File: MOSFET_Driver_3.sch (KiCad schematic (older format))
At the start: 20 parts, among them Q10 TPHR8504PL, Q11 TPHR8504PL, Q12 TPHR8504PL, Q7 TPHR8504PL, Q8 TPHR8504PL, Q9 TPHR8504PL, U1 FD6288Q

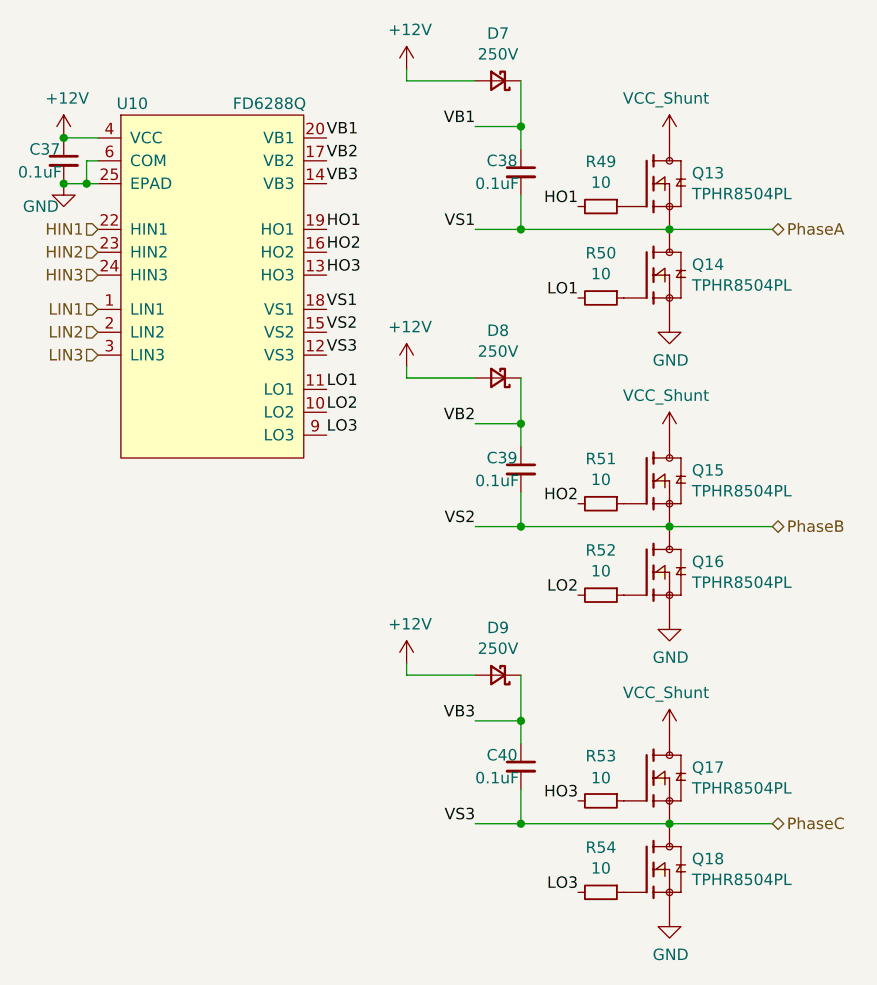
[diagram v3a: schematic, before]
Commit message: Finished all traces and vias
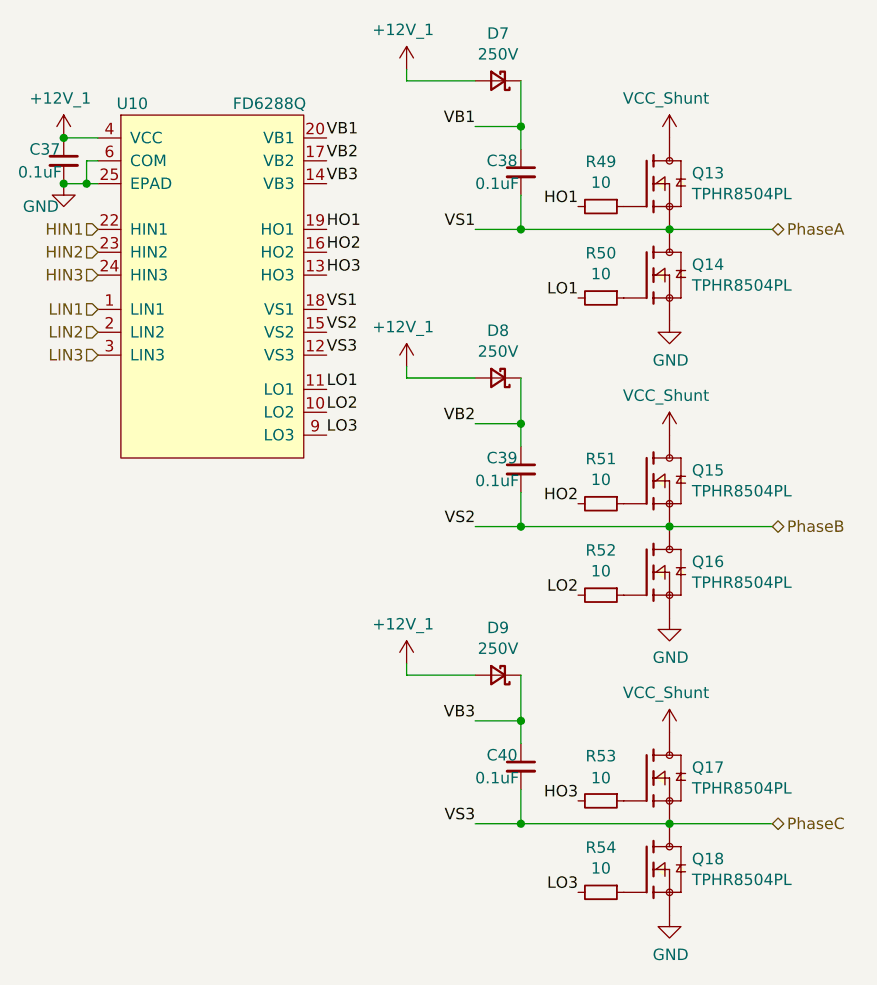
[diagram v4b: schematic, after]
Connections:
- net +12V renamed +12V_1
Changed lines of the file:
@@
 	7500 4850 7500 5000
 Connection ~ 7500 5000
-$Comp
-L power:+12V #PWR02
-U 1 1 6059DFDF
-P 5500 2000
-AR Path="/6035042B/6059DFDF" Ref="#PWR02"  Part="1"
-AR Path="/605793F0/6059DFDF" Ref="#PWR0140"  Part="1"
-AR Path="/6057AB51/6059DFDF" Ref="#PWR0169"  Part="1"
-AR Path="/60597CFF/6059DFDF" Ref="#PWR?"  Part="1"
-AR Path="/60568CDE/6059DFDF" Ref="#PWR0184"  Part="1"
-AR Path="/60595220/6059DFDF" Ref="#PWR0184"  Part="1"
-AR Path="/605CA83C/6059DFDF" Ref="#PWR0184"  Part="1"
-AR Path="/605DC768/6059DFDF" Ref="#PWR0209"  Part="1"
-AR Path="/60536007/6059DFDF" Ref="#PWR0196"  Part="1"
-AR Path="/60551876/6059DFDF" Ref="#PWR0227"  Part="1"
-F 0 "#PWR0196" H 5500 1850 50  0001 C CNN
-F 1 "+12V" H 5515 2173 50  0000 C CNN
-F 2 "" H 5500 2000 50  0001 C CNN
-F 3 "" H 5500 2000 50  0001 C CNN
-	1    5500 2000
-	1    0    0    -1
-$EndComp
-$Comp
-L power:+12V #PWR03
-U 1 1 6059DFE7
-P 7000 3000
-AR Path="/6035042B/6059DFE7" Ref="#PWR03"  Part="1"
-AR Path="/605793F0/6059DFE7" Ref="#PWR0141"  Part="1"
-AR Path="/6057AB51/6059DFE7" Ref="#PWR0170"  Part="1"
-AR Path="/60597CFF/6059DFE7" Ref="#PWR?"  Part="1"
-AR Path="/60568CDE/6059DFE7" Ref="#PWR0185"  Part="1"
-AR Path="/60595220/6059DFE7" Ref="#PWR0185"  Part="1"
-AR Path="/605CA83C/6059DFE7" Ref="#PWR0185"  Part="1"
-AR Path="/605DC768/6059DFE7" Ref="#PWR0210"  Part="1"
-AR Path="/60536007/6059DFE7" Ref="#PWR0197"  Part="1"
-AR Path="/60551876/6059DFE7" Ref="#PWR0228"  Part="1"
-F 0 "#PWR0197" H 7000 2850 50  0001 C CNN
-F 1 "+12V" H 7015 3173 50  0000 C CNN
-F 2 "" H 7000 3000 50  0001 C CNN
-F 3 "" H 7000 3000 50  0001 C CNN
-	1    7000 3000
-	1    0    0    -1
-$EndComp
-$Comp
-L power:+12V #PWR01
-U 1 1 6057ED65
-P 7000 1700
-AR Path="/6035042B/6057ED65" Ref="#PWR01"  Part="1"
-AR Path="/605793F0/6057ED65" Ref="#PWR0142"  Part="1"
-AR Path="/6057AB51/6057ED65" Ref="#PWR0171"  Part="1"
-AR Path="/60597CFF/6057ED65" Ref="#PWR?"  Part="1"
-AR Path="/60568CDE/6057ED65" Ref="#PWR0186"  Part="1"
-AR Path="/60595220/6057ED65" Ref="#PWR0186"  Part="1"
-AR Path="/605CA83C/6057ED65" Ref="#PWR0186"  Part="1"
-AR Path="/605DC768/6057ED65" Ref="#PWR0211"  Part="1"
-AR Path="/60536007/6057ED65" Ref="#PWR0198"  Part="1"
-AR Path="/60551876/6057ED65" Ref="#PWR0229"  Part="1"
-F 0 "#PWR0198" H 7000 1550 50  0001 C CNN
-F 1 "+12V" H 7015 1873 50  0000 C CNN
-F 2 "" H 7000 1700 50  0001 C CNN
-F 3 "" H 7000 1700 50  0001 C CNN
-	1    7000 1700
-	1    0    0    -1
-$EndComp
-$Comp
-L power:+12V #PWR04
-U 1 1 6057ED66
-P 7000 4300
-AR Path="/6035042B/6057ED66" Ref="#PWR04"  Part="1"
-AR Path="/605793F0/6057ED66" Ref="#PWR0143"  Part="1"
-AR Path="/6057AB51/6057ED66" Ref="#PWR0172"  Part="1"
-AR Path="/60597CFF/6057ED66" Ref="#PWR?"  Part="1"
-AR Path="/60568CDE/6057ED66" Ref="#PWR0187"  Part="1"
-AR Path="/60595220/6057ED66" Ref="#PWR0187"  Part="1"
-AR Path="/605CA83C/6057ED66" Ref="#PWR0187"  Part="1"
-AR Path="/605DC768/6057ED66" Ref="#PWR0212"  Part="1"
-AR Path="/60536007/6057ED66" Ref="#PWR0199"  Part="1"
-AR Path="/60551876/6057ED66" Ref="#PWR0230"  Part="1"
-F 0 "#PWR0199" H 7000 4150 50  0001 C CNN
-F 1 "+12V" H 7015 4473 50  0000 C CNN
-F 2 "" H 7000 4300 50  0001 C CNN
-F 3 "" H 7000 4300 50  0001 C CNN
-	1    7000 4300
-	1    0    0    -1
-$EndComp
 $Bitmap
 Pos 4150 2500
@@
 Wire Wire Line
 	5500 2000 5650 2000
-Connection ~ 5500 2000
 Wire Wire Line
 	5650 2200 5600 2200
@@
 	1    0    0    -1
 $EndComp
+$Comp
+L power:+12V_1 #PWR0177
+U 1 1 606F7034
+P 5500 2000
+F 0 "#PWR0177" H 5500 1900 50  0001 C CNN
+F 1 "+12V_1" H 5485 2173 50  0000 C CNN
+F 2 "" H 5500 2000 50  0001 C CNN
+F 3 "" H 5500 2000 50  0001 C CNN
+	1    5500 2000
+	1    0    0    -1
+$EndComp
+Connection ~ 5500 2000
+$Comp
+L power:+12V_1 #PWR0196
+U 1 1 606F7857
+P 7000 1700
+F 0 "#PWR0196" H 7000 1600 50  0001 C CNN
+F 1 "+12V_1" H 6985 1873 50  0000 C CNN
+F 2 "" H 7000 1700 50  0001 C CNN
+F 3 "" H 7000 1700 50  0001 C CNN
+	1    7000 1700
+	1    0    0    -1
+$EndComp
+$Comp
+L power:+12V_1 #PWR0197
+U 1 1 606F7D88
+P 7000 3000
+F 0 "#PWR0197" H 7000 2900 50  0001 C CNN
+F 1 "+12V_1" H 6985 3173 50  0000 C CNN
+F 2 "" H 7000 3000 50  0001 C CNN
+F 3 "" H 7000 3000 50  0001 C CNN
+	1    7000 3000
+	1    0    0    -1
+$EndComp
+$Comp
+L power:+12V_1 #PWR0198
+U 1 1 606F82E3
+P 7000 4300
+F 0 "#PWR0198" H 7000 4200 50  0001 C CNN
+F 1 "+12V_1" H 6985 4473 50  0000 C CNN
+F 2 "" H 7000 4300 50  0001 C CNN
+F 3 "" H 7000 4300 50  0001 C CNN
+	1    7000 4300
+	1    0    0    -1
+$EndComp
